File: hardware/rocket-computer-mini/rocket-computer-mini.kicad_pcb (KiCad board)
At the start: 6 copper layers, 22 x 54.8 mm, 156 parts, among them J2 TBLH11-350-05-BK, J3 JST_B2B-PH-SM4-TB, J6 USB4110GFA, J8 CON-SMA-EDGE-S, Q11 AONR21321, Q3 DTC123J, Q4 DTC123J, Q5 DTC123J, Q6 DTC123J, SW3 R-667995, U10 WSD20L50DN33, U11 GD5F1GQ5UEYIGR, U13 GD25Q128ESIG, U15 ESP32-S3RH2, U16 E220-900MM22S, U18 TPS62152RGTR, U19 TPS259631DDAR, U2 ISM6HG256XTR, U21 TPS2121RUXR, U23 INA230AIRGTR, U3 QMC5883P, U30 TPS22810DRVR, U31 ANT016008LCS2442MA2, U4 BMP581, U5 LC86GLAMD, U6 WSD20L50DN33, U7 WSD20L50DN33, U8 WSD20L50DN33, U9 AON7534, Y1 ABS07-32.768KHZ-T, Y2 ECS-400-10-37B2-CKY-TR

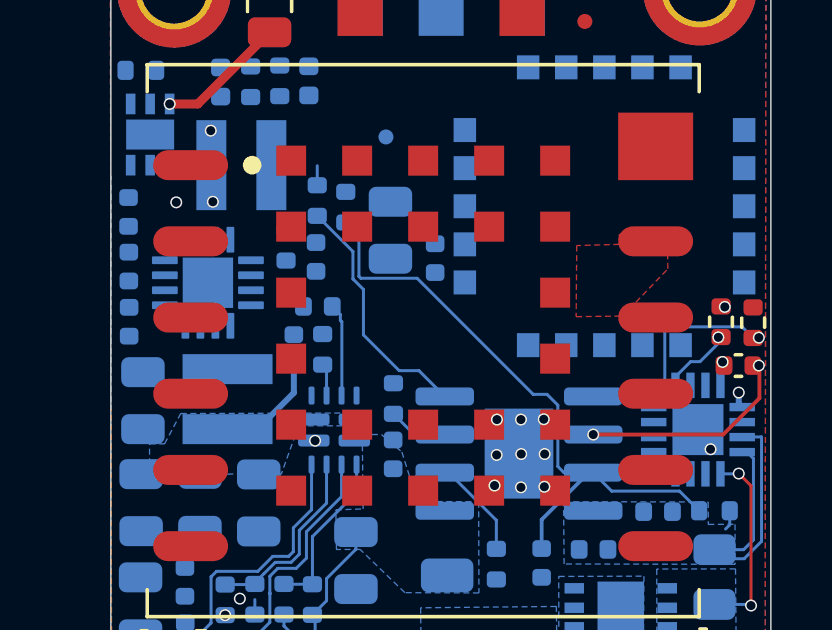
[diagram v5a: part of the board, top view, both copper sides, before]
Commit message: mini: the magnetometer belongs to the flight computer
It is a flight sensor and it was on the wrong processor. The IMU, the
barometer and the GNSS all sit on the flight computer; the magnetometer
alone hung off the out computer's power-monitor I2C bus. That was a
single-MCU decision -- pin-budget.md's "shares the power-monitor I2C bus,
no new pins" -- and nothing revisited it when the board grew a second
processor. rocket-computer has always put its IIS2MDCTR on the flight
computer's own bus with the pull-ups on the same rail as the part.

Being stranded there broke it in two independent ways:

  * Electrically. R67/R69 pull up to +3V3 while U3's supply sat behind U30,
    whose QOD ACTIVELY discharges the rail. In pad standby those pull-ups
    drove its I2C pads against a grounded supply -- above abs-max, clamping
    the bus below VIL, and making the INA230 unreadable. That is the whole
    of the board's battery telemetry; nothing else reaches VBAT.
  * In firmware. Every magnetometer driver in the tree is built into
    flight_computer, which cannot reach a part on the other processor's
    bus, so the board had no heading source at all.

The previous commit addressed only the first, by moving U3's supply to
+3V3. That treated the symptom -- correct as far as it went, but it left a
flight sensor on the comms processor. This moves the part instead:

  U3 SCL/SDA  -> MAG_SCL / MAG_SDA on the FC, GPIO37 / GPIO36
  R117/R118   -> 5.11 k pull-ups on V_MCU_SWTCH, the part's own rail
  U3 VDD      -> back to V_MCU_SWTCH with the other three sensors
  SEN_SCL/SDA -> pure pack-monitor bus on +3V3 (U15 + U23 + R67/R69),
                 the same shape as rocket-computer's PWR_SCL/PWR_SDA

Now the part, its master and its pull-ups all share one rail, so no passive
pull-up crosses the rail boundary at all -- every remaining crossing is an
actively driven signal firmware can park Hi-Z.

Firmware follows: flight_computer/board_m1.h gets IIS2MDC_SDA=36,
IIS2MDC_SCL=37 and USE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
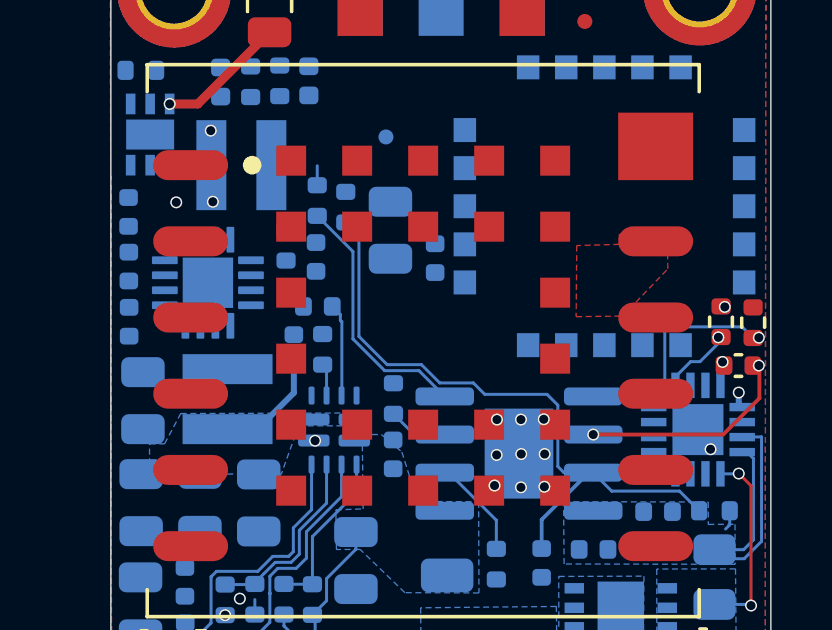
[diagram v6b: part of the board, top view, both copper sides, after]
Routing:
- net Net-(U19-EN/UVLO): track 21.2 -> 22.4 mm
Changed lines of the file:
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@@
 	)
 	(segment
-		(start 83.11 131.54)
-		(end 82.451527 131.54)
-		(width 0.1)
-		(layer "B.Cu")
-		(net "Net-(U19-OVLO)")
-	)
-	(segment
-		(start 81.26 128.832842)
-		(end 80.91 128.482842)
-		(width 0.1)
-		(layer "B.Cu")
-		(net "Net-(U19-OVLO)")
-	)
-	(segment
-		(start 80.91 128.482842)
-		(end 80.91 127.57)
-		(width 0.1)
-		(layer "B.Cu")
-		(net "Net-(U19-OVLO)")
-	)
-	(segment
-		(start 82.451527 131.54)
-		(end 81.26 130.348473)
+		(start 81.967157 131.54)
+		(end 80.91 130.482842)
 		(width 0.1)
 		(layer "B.Cu")
@@
 	)
 	(segment
-		(start 81.26 130.348473)
-		(end 81.26 128.832842)
+		(start 83.11 131.54)
+		(end 81.967157 131.54)
 		(width 0.1)
 		(layer "B.Cu")
@@
 	)
 	(segment
+		(start 80.91 130.482842)
+		(end 80.91 127.57)
+		(width 0.1)
+		(layer "B.Cu")
+		(net "Net-(U19-OVLO)")
+	)
+	(segment
+		(start 83.192842 131.34)
+		(end 82.05 131.34)
+		(width 0.1)
+		(layer "B.Cu")
+		(net "Net-(U19-EN{slash}UVLO)")
+	)
+	(segment
 		(start 87.38 132.33)
-		(end 86.918473 132.33)
+		(end 85.30342 132.33)
+		(width 0.1)
+		(layer "B.Cu")
+		(net "Net-(U19-EN{slash}UVLO)")
+	)
+	(segment
+		(start 88.92 134.94)
+		(end 87.945001 134.94)
+		(width 0.1)
+		(layer "B.Cu")
+		(net "Net-(U19-EN{slash}UVLO)")
+	)
+	(segment
+		(start 84.92342 131.95)
+		(end 83.802842 131.95)
 		(width 0.1)
 		(layer "B.Cu")
@@
 	)
 	(segment
-		(start 87.74 132.69)
-		(end 87.38 132.33)
-		(width 0.1)
-		(layer "B.Cu")
-		(net "Net-(U19-EN{slash}UVLO)")
-	)
-	(segment
-		(start 88.92 134.94)
-		(end 87.945001 134.94)
+		(start 87.945001 134.94)
+		(end 87.74 134.734999)
 		(width 0.1)
 		(layer "B.Cu")
@@
 	)
 	(segment
-		(start 87.74 134.734999)
-		(end 87.74 132.69)
+		(start 91.795002 135.555002)
+		(end 89.535002 135.555002)
+		(width 0.1)
+		(layer "B.Cu")
+		(net "Net-(U19-EN{slash}UVLO)")
+	)
+	(segment
+		(start 83.802842 131.95)
+		(end 83.192842 131.34)
+		(width 0.1)
+		(layer "B.Cu")
+		(net "Net-(U19-EN{slash}UVLO)")
+	)
+	(segment
+		(start 87.2 137.47)
+		(end 87.2 136.507488)
+		(width 0.127)
+		(layer "B.Cu")
+		(net "Net-(U19-EN{slash}UVLO)")
+	)
+	(segment
+		(start 82.05 131.34)
+		(end 81.11 130.4)
 		(width 0.1)
 		(layer "B.Cu")
@@
 	)
 	(segment
-		(start 91.795002 135.555002)
-		(end 89.535002 135.555002)
-		(width 0.1)
-		(layer "B.Cu")
-		(net "Net-(U19-EN{slash}UVLO)")
-	)
-	(segment
-		(start 87.2 137.47)
-		(end 87.2 136.507488)
+		(start 87.2 136.507488)
+		(end 88.767488 134.94)
 		(width 0.127)
 		(layer "B.Cu")
@@
 	)
 	(segment
-		(start 87.2 136.507488)
-		(end 88.767488 134.94)
-		(width 0.127)
+		(start 85.30342 132.33)
+		(end 84.92342 131.95)
+		(width 0.1)
 		(layer "B.Cu")
 		(net "Net-(U19-EN{slash}UVLO)")
@@
 	)
 	(segment
-		(start 81.11 128.4)
+		(start 81.11 130.4)
 		(end 81.11 127.04)
-		(width 0.1)
-		(layer "B.Cu")
-		(net "Net-(U19-EN{slash}UVLO)")
-	)
-	(segment
-		(start 87.945001 134.94)
-		(end 87.74 134.734999)
-		(width 0.1)
-		(layer "B.Cu")
-		(net "Net-(U19-EN{slash}UVLO)")
-	)
-	(segment
-		(start 86.918473 132.33)
-		(end 83.048473 128.46)
-		(width 0.1)
-		(layer "B.Cu")
-		(net "Net-(U19-EN{slash}UVLO)")
-	)
-	(segment
-		(start 83.048473 128.46)
-		(end 81.17 128.46)
-		(width 0.1)
-		(layer "B.Cu")
-		(net "Net-(U19-EN{slash}UVLO)")
-	)
-	(segment
-		(start 81.17 128.46)
-		(end 81.11 128.4)
 		(width 0.1)
 		(layer "B.Cu")
@@
 		(width 0.1)
 		(layer "B.Cu")
+		(net "Net-(U19-EN{slash}UVLO)")
+	)
+	(segment
+		(start 87.74 132.69)
+		(end 87.38 132.33)
+		(width 0.1)
+		(layer "B.Cu")
+		(net "Net-(U19-EN{slash}UVLO)")
+	)
+	(segment
+		(start 87.74 134.734999)
+		(end 87.74 132.69)
+		(width 0.1)
+		(layer "B.Cu")

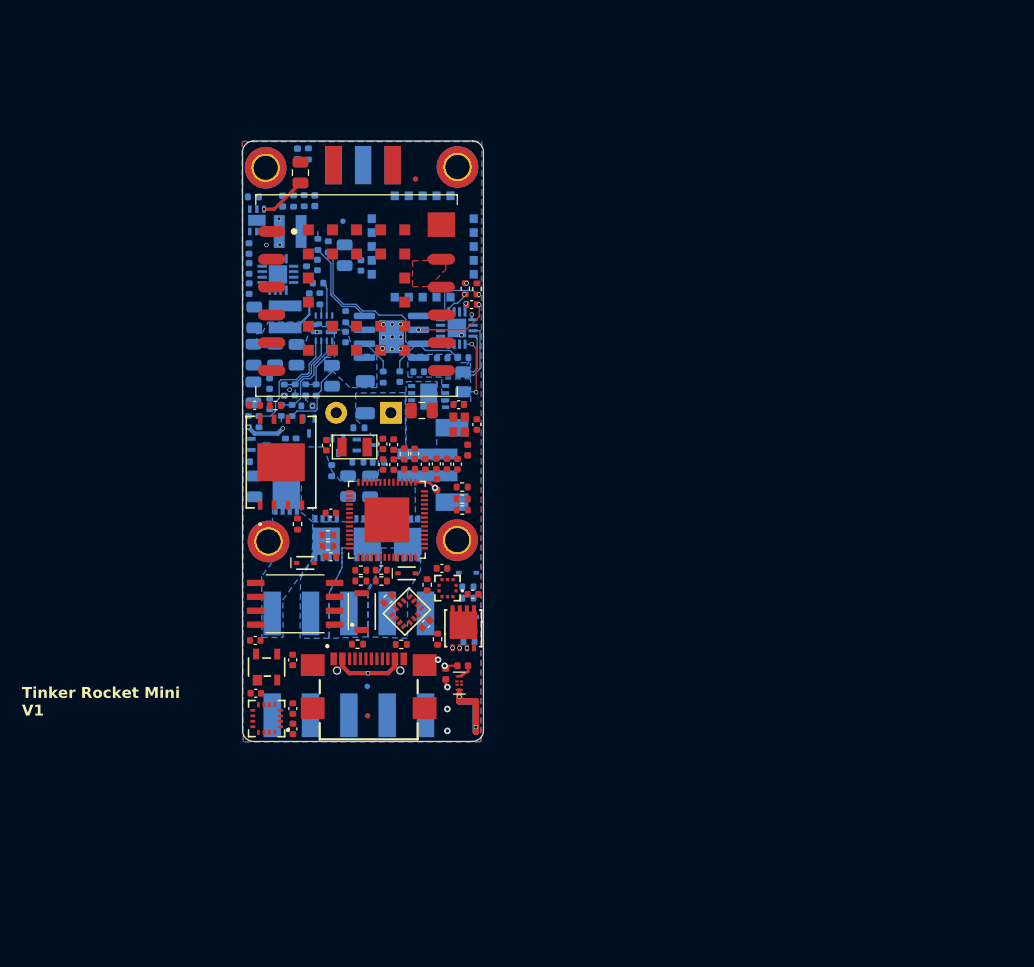
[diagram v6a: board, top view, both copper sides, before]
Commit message: hardware: pack-direct pyro + supercap hold-up on both rocket computers (WIP)
rocket-computer-mini:
- pyro store deleted; channels fire from VBAT_CON (pack-direct, upstream
  of the 0.9 A eFuse). PYRO_FIRE_DURATION is a live knob again.
- ARM is a charge-pump dead-man (ARM_CLK on FC GPIO8, ex-PYRO_ARM; a
  static GPIO can never arm) with a latching hardware ceiling that times
  ARM_GATE itself (1.5-3.3 s; release = FC-domain power cycle).
- +3V3 hold-up: V_BUCK -> LM66100 -> V_HOLD -> TPS22810 -> +3V3 with a
  2 F supercap (CHP5R5L205R-TWQ) behind 33R charge / LM66100 discharge,
  TPS3840PL29 cutting cleanly at 2.86-2.94 V. Both LM66100 CE pins tie
  to VOUT (reverse blocking); U40 ST is CAP_ACTIVE (low=buck, high=cap).
- DEF tied to V_BUCK (3.465 V rail); CAP_ACTIVE to both MCUs;
  V_SCAP_ADC on OC GPIO8. Console UART fully restored.
- PCB re-synced to the schematic; 76 dangling P4-era segments/vias and
  6 dead zones purged, all fills regenerated (97 stale-fill clearance
  violations cleared); schematic parity: 0 violations. No outline yet.

rocket-computer (V10): same architecture drawn as off-page blocks with
the same refdes; 2x supercaps for the 0.5-0.8 A dual-MCU load; V_CAP ->
VBAT_CON; C94 1u -> 4.7u so a 500 ms firing sag cannot open the eFuse
(GNSS daughterboards ride the raw sag; TPS62913 input floor ~3.8 V).
P4 pad 17 = ARM_CLK, pad 18 = V_SCAP_ADC, PIEZZO moved to the S3.
MANUAL: the V_BUCK rail split at U18 (note on the power sheet).

docs: firmware-notes.md (BOD to 2.44 V both MCUs, CAP_ACTIVE handler,
shed order, ARM spacing) and pack-fire-holdup-options.md (options A-D,
complications register). New prismatic supercap footprint; shared
footprint refreshes from the KiCad sessions.

Both boards are WIP: mini layout not started, V10 splice pending.

Co-Authored-By: Claude Fable 5 <noreply@anthropic.com>
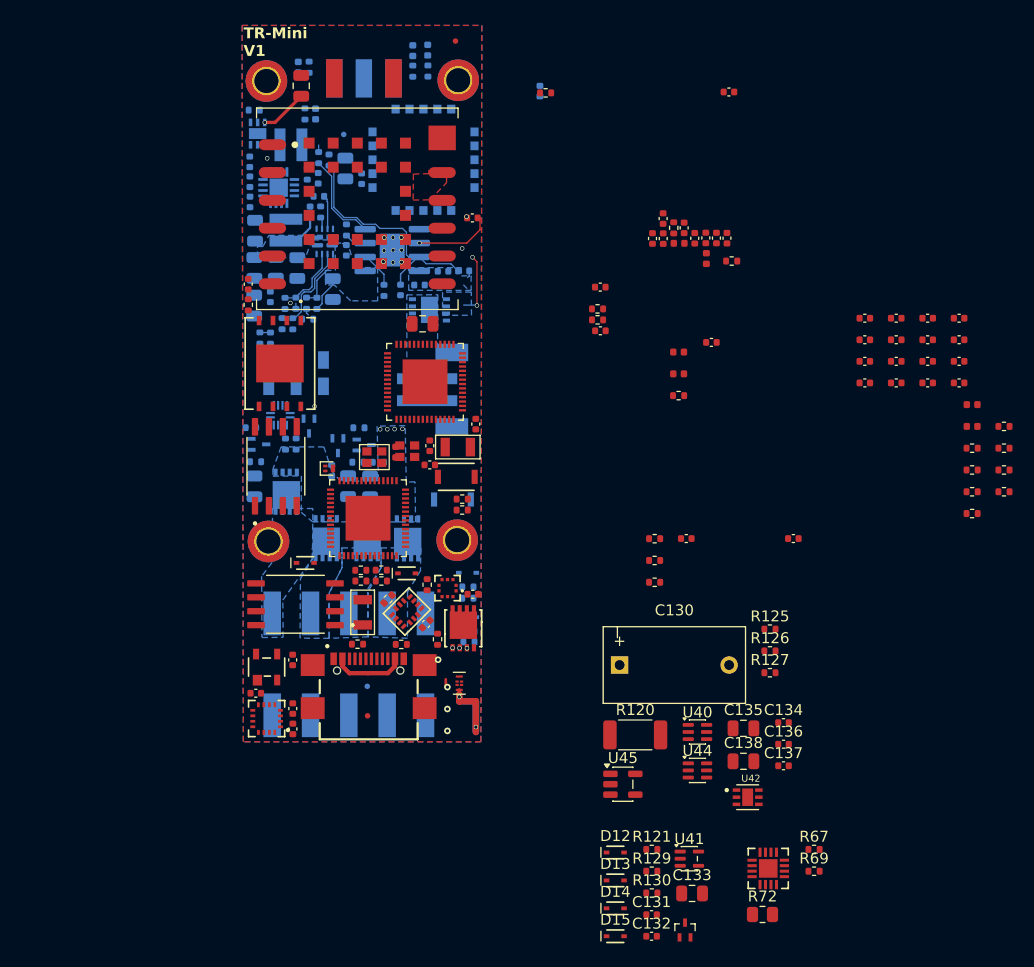
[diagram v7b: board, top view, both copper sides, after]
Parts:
- removed C12: 2200uF 16V, Footprints:CP_Radial_D12.5mm_L20.0mm_P5.00mm_Horizontal_Strap
- removed D8: White, LED_SMD:LED_0402_1005Metric
- removed R20: 150 - CRCW1206-HP, Resistor_SMD:R_1206_3216Metric
- removed R68: 10 k, Resistor_SMD:R_0402_1005Metric
- added C1: 100 nF, Capacitor_SMD:C_0402_1005Metric, F.Cu at (113.4, 152.7)
- added C105: 10 uF, Capacitor_SMD:C_0402_1005Metric, F.Cu at (123.1, 152.7)
- added C110: 22 pF, Capacitor_SMD:C_0402_1005Metric, F.Cu at (129.7, 132.6)
- added C111: 22 pF, Capacitor_SMD:C_0402_1005Metric, F.Cu at (129.7, 134.6)
- added C112: 12 pF, Capacitor_SMD:C_0402_1005Metric, F.Cu at (129.7, 136.6)
- added C113: 12 pF, Capacitor_SMD:C_0402_1005Metric, F.Cu at (129.7, 138.5)
- added C114: 1 uF, Capacitor_SMD:C_0402_1005Metric, F.Cu at (132.5, 132.6)
- added C115: 100 nF, Capacitor_SMD:C_0402_1005Metric, F.Cu at (132.5, 134.6)
- added C116: 1 uF, Capacitor_SMD:C_0402_1005Metric, F.Cu at (132.5, 136.6)
- added C117: 10 nF, Capacitor_SMD:C_0402_1005Metric, F.Cu at (132.5, 138.5)
- added C118: 100 nF, Capacitor_SMD:C_0402_1005Metric, F.Cu at (135.4, 132.6)
- added C119: 1 uF, Capacitor_SMD:C_0402_1005Metric, F.Cu at (135.4, 134.6)
- added C120: 100 nF, Capacitor_SMD:C_0402_1005Metric, F.Cu at (135.4, 136.6)
- added C121: 10 uF, Capacitor_SMD:C_0402_1005Metric, F.Cu at (135.4, 138.5)
- added C122: 100 nF, Capacitor_SMD:C_0402_1005Metric, F.Cu at (138.3, 132.6)
- added C123: 100 nF, Capacitor_SMD:C_0402_1005Metric, F.Cu at (138.3, 134.6)
- added C124: 1 uF, Capacitor_SMD:C_0402_1005Metric, F.Cu at (138.3, 136.6)
- added C125: 10 uF, Capacitor_SMD:C_0402_1005Metric, F.Cu at (138.3, 138.5)
- added C130: CHP5R5L205R-TWQ, Footprints:Supercap_Prismatic_13.0x7.0mm_H28.5mm_P10.00mm, F.Cu at (112.3, 164.3)
- added C131: 100 nF, Capacitor_SMD:C_0402_1005Metric, F.Cu at (110.2, 187.1)
- added C132: 1 uF, Capacitor_SMD:C_0402_1005Metric, F.Cu at (110.2, 189.1)
- added C133: 10 uF, Capacitor_SMD:C_0805_2012Metric, F.Cu at (113.9, 185.1)
- added C134: 10 nF, Capacitor_SMD:C_0402_1005Metric, F.Cu at (122.2, 169.5)
- added C135: 22 uF, Capacitor_SMD:C_0805_2012Metric, F.Cu at (118.6, 170.1)
- added C136: 10 nF, Capacitor_SMD:C_0402_1005Metric, F.Cu at (122.2, 171.5)
- added C137: 100 nF, Capacitor_SMD:C_0402_1005Metric, F.Cu at (122.2, 173.5)
- added C138: 10 uF, Capacitor_SMD:C_0805_2012Metric, F.Cu at (118.6, 173.1)
- added D10: Red, LED_SMD:LED_0402_1005Metric, B.Cu at (88.4, 108.2)
- added D11: Blue, LED_SMD:LED_0402_1005Metric, B.Cu at (89.8, 108.1)
- added D12: BAT54XV2T1G, Footprints:SOD-523_0P9X1P3_ONS, F.Cu at (106.9, 181.4)
- added D13: BAT54XV2T1G, Footprints:SOD-523_0P9X1P3_ONS, F.Cu at (106.9, 184.0)
- added D14: BAT54XV2T1G, Footprints:SOD-523_0P9X1P3_ONS, F.Cu at (106.9, 186.5)
- added D15: BAT54XV2T1G, Footprints:SOD-523_0P9X1P3_ONS, F.Cu at (106.9, 189.1)
- added D9: BAV170M, Package_TO_SOT_SMD:SOT-883, F.Cu at (80.8, 146.3)
- added L10: 2 nH, Inductor_SMD:L_0402_1005Metric, F.Cu at (139.5, 142.5)
- added L9: 24 nH, Inductor_SMD:L_0402_1005Metric, F.Cu at (139.5, 140.5)
- added Q12: DTC123J, Footprints:DTC123JEBTL, F.Cu at (113.2, 188.5)
- added R1: 100 k, Resistor_SMD:R_0402_1005Metric, F.Cu at (110.5, 152.7)
- added R110: 10 k, Resistor_SMD:R_0402_1005Metric, F.Cu at (139.5, 144.5)
- added R111: 10 k, Resistor_SMD:R_0402_1005Metric, F.Cu at (139.5, 146.5)
- added R112: 22, Resistor_SMD:R_0402_1005Metric, F.Cu at (139.5, 148.5)
- added R113: 22, Resistor_SMD:R_0402_1005Metric, F.Cu at (139.5, 150.4)
- added R115: 5.11 k, Resistor_SMD:R_0402_1005Metric, F.Cu at (142.4, 142.5)
- added R116: 5.11 k, Resistor_SMD:R_0402_1005Metric, F.Cu at (142.4, 144.5)
- added R117: 5.11 k, Resistor_SMD:R_0402_1005Metric, F.Cu at (142.4, 146.5)
- added R118: 5.11 k, Resistor_SMD:R_0402_1005Metric, F.Cu at (142.4, 148.5)
- added R120: 33 - 0.5 W, Resistor_SMD:R_2010_5025Metric, F.Cu at (108.7, 170.7)
- added R121: 1 M, Resistor_SMD:R_0402_1005Metric, F.Cu at (110.2, 181.1)
- added R125: 100 k, Resistor_SMD:R_0402_1005Metric, F.Cu at (121.0, 161.0)
- added R126: 100 k, Resistor_SMD:R_0402_1005Metric, F.Cu at (121.0, 163.0)
- added R127: 100 k, Resistor_SMD:R_0402_1005Metric, F.Cu at (121.0, 165.0)
- added R129: 10 k, Resistor_SMD:R_0402_1005Metric, F.Cu at (110.2, 183.1)
- added R130: 22 k, Resistor_SMD:R_0402_1005Metric, F.Cu at (110.2, 185.1)
- added R2: 100 k, Resistor_SMD:R_0402_1005Metric, F.Cu at (110.5, 154.7)
- added R3: 22, Resistor_SMD:R_0402_1005Metric, F.Cu at (110.5, 156.7)
- added R34: 100 k, Resistor_SMD:R_0402_1005Metric, F.Cu at (112.7, 139.7)
- added R70: 10 k, Resistor_SMD:R_0402_1005Metric, B.Cu at (88.4, 110.0)
- added R71: 10 k, Resistor_SMD:R_0402_1005Metric, B.Cu at (89.8, 110.0)
- added S1: JS202011JCQN, Footprints:SW_JS202011JCQN, B.Cu at (77.7, 137.6)
- added SW2: R-667995, Footprints:R-667995_MIT, B.Cu at (92.0, 149.2)
- added U1: FSUSB63UMX, Footprints:QFN40P180X180X55-12N, B.Cu at (76.3, 141.5)
- added U32: ESP32-S3RH2, Footprints:IC_ESP32-S3, F.Cu at (84.3, 150.9)
- added U33: GD25Q128ESIG, Footprints:SOIC127P790X216-8N, F.Cu at (77.7, 158.7)
- added U40: LM66100DCK, Package_TO_SOT_SMD:SOT-363_SC-70-6, F.Cu at (114.4, 170.4)
- added U41: 74LVC1G17, Package_TO_SOT_SMD:SOT-353_SC-70-5, F.Cu at (113.6, 182.0)
- added U42: TPS22810DRVR, Footprints:SON65P200X200X80-7N, F.Cu at (119.0, 176.4)
- added U44: LM66100DCK, Package_TO_SOT_SMD:SOT-363_SC-70-6, F.Cu at (114.4, 173.9)
- added U45: TPS3840PL29, Package_TO_SOT_SMD:SOT-23-5, F.Cu at (107.6, 175.2)
- added Y3: ABS07-32.768KHZ-T, Footprints:XTAL_SC-32S_3215, F.Cu at (83.8, 159.5)
- added Y4: ECS-400-10-37B2-CKY-TR, Footprints:XTAL_ECS-400-10-37B2-CKY-TR, F.Cu at (84.9, 145.3)
- C26: moved to B.Cu
- R72, U23: moved to F.Cu
- moved R69 61.4 mm to (125.0, 183.1), turned to 0 degrees
- moved R67 60.3 mm to (125.0, 181.1), turned to 0 degrees
- moved U23 57.0 mm to (120.9, 182.9)
- moved R72 55.8 mm to (120.3, 187.1), turned to 0 degrees
- moved C16 37.7 mm to (100.0, 111.9)
- moved C22 37.7 mm to (117.3, 112.0)
- moved R31 37.7 mm to (100.5, 112.0)
- moved L7 34.8 mm to (112.7, 135.7)
- moved L8 34.7 mm to (112.7, 137.7), turned to 0 degrees
- moved C27 32.1 mm to (105.5, 133.8)
- moved C31 32.1 mm to (115.7, 134.8)
- moved L1 32.1 mm to (115.2, 127.2)
- moved R38 32.1 mm to (105.3, 132.8)
- moved R39 32.1 mm to (105.3, 131.8)
- moved C25 32.1 mm to (113.2, 124.4)
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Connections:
- net /MCU - ESP32-S3/ANT_FEED renamed /MCU - ESP32-S3 Out Computer/ANT_FEED
- net MCU_SPI_CLK renamed OC_SPI_CLK
- net MCU_SPI_CS0 renamed OC_SPI_CS0
- net MCU_SPI_D renamed OC_SPI_D
- net MCU_SPI_HD renamed OC_SPI_HD
- net MCU_SPI_Q renamed OC_SPI_Q
- net MCU_SPI_WP renamed OC_SPI_WP
- net MCU_VDD_SPI renamed OC_VDD_SPI
- C10 pad 1: V_CAP -> VBAT_CON
- C11 pad 1: V_CAP -> VBAT_CON
- C13 pad 1: V_CAP -> VBAT_CON
- C53 pad 1: +3V3 -> V_BUCK
- C9 pad 1: V_CAP -> VBAT_CON
- L6 pad 2: +3V3 -> V_BUCK
- R15 pad 2: V_CAP -> VBAT_CON
- R16 pad 2: V_CAP -> VBAT_CON
- R17 pad 2: V_CAP -> VBAT_CON
- R21 pad 2: PYRO_ARM -> ARM_GATE
- R23 pad 2: V_CAP -> VBAT_CON
- R38 pad 1: D+ -> OC_D+
- R39 pad 1: D- -> OC_D-
- R49 pad 2: +3V3 -> V_BUCK
- R65 pad 1: +3V3 -> V_BUCK
- U10 pad 1: V_CAP -> VBAT_CON
- U10 pad 2: V_CAP -> VBAT_CON
- U10 pad 3: V_CAP -> VBAT_CON
- U15 pad 10: PYRO2_FIRE -> ESP_SDA
- U15 pad 11: PYRO3_FIRE -> ESP_SCL
- U15 pad 12: PYRO4_FIRE -> FC_EN_OC
- U15 pad 13: PYRO_ARM -> V_SCAP_ADC
- U15 pad 14: ISM6HG256_CS -> unconnected-(U15-GPIO9-Pad14)
- U15 pad 15: PYRO1_CONT -> unconnected-(U15-GPIO10-Pad15)
- U15 pad 16: PYRO2_CONT -> unconnected-(U15-GPIO11-Pad16)
- U15 pad 17: PYRO3_CONT -> unconnected-(U15-GPIO12-Pad17)
- U15 pad 36: BMP585_CS -> unconnected-(U15-SPICLK_N-Pad36)
- U15 pad 37: ISM6HG256_INT1 -> unconnected-(U15-SPICLK_P-Pad37)
- U15 pad 39: SENS_SCLK -> CAP_ACTIVE
- U15 pad 44: GNSS_TX -> unconnected-(U15-MTCK-Pad44)
- U15 pad 45: GNSS_RX -> unconnected-(U15-MTDO-Pad45)
- U15 pad 47: BMP585_INT -> unconnected-(U15-MTDI-Pad47)
- U15 pad 48: PYRO4_CONT -> unconnected-(U15-MTMS-Pad48)
- U15 pad 51: Net-(U15-GPIO45) -> unconnected-(U15-GPIO45-Pad51)
- U15 pad 6: SENS_SDI -> ESP_CS
- U15 pad 7: SENS_SDO -> ESP_SCLK
- U15 pad 8: POWER_SWITCH -> ESP_SDO
- U15 pad 9: PYRO1_FIRE -> ESP_SDI
- U18 pad 14: +3V3 -> V_BUCK
- U18 pad 7: +3V3 -> V_BUCK
- U18 pad 8: GND -> V_BUCK
- U3 pad 1: SEN_SCL -> MAG_SCL
- U3 pad 16: SEN_SDA -> MAG_SDA
- U6 pad 1: V_CAP -> VBAT_CON
- U6 pad 2: V_CAP -> VBAT_CON
- U6 pad 3: V_CAP -> VBAT_CON
- U7 pad 1: V_CAP -> VBAT_CON
- U7 pad 2: V_CAP -> VBAT_CON
- U7 pad 3: V_CAP -> VBAT_CON
- U8 pad 1: V_CAP -> VBAT_CON
- U8 pad 2: V_CAP -> VBAT_CON
- U8 pad 3: V_CAP -> VBAT_CON
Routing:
- net Net-(J6-VBUS): track 51.5 -> 6.67 mm, vias 5 -> 0
- net +3V3: track 27.2 -> 4.32 mm, vias 5 -> 1
- net /MCU - ESP32-S3 Out Computer/ANT_FEED: track 21.4 -> 0.00 mm, vias 2 -> 0
- net GND: track 15.8 -> 3.42 mm
- net Net-(U21-PR1): track 11.7 -> 0.96 mm
- net VBAT_CON: track 11.0 -> 1.10 mm, vias 0 -> 4
- net SEN_SDA: track 6.08 -> 0.00 mm, vias 1 -> 0
- net VBATT: track 7.19 -> 3.49 mm
- net SEN_SCL: track 2.43 -> 0.00 mm, vias 1 -> 0
- net Net-(U31-FEED): track 1.46 -> 0.00 mm
- net Net-(U21-OV2): track 8.63 -> 7.47 mm
- net VBAT_Terminal: track 6.42 -> 5.82 mm
- net Net-(U19-dVdt): vias 2 -> 1
- added copper zone on In2.Cu, net VBAT_CON
- removed copper zone on B.Cu, net V_CAP
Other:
- board outline removed
- board text added: "TR-Mini ${REVISION}"
- board text removed: "Tinker Rocket Mini ${REVISION}"
